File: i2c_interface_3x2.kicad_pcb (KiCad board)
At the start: 2 copper layers, 70.5 x 41.9 mm, 1 part

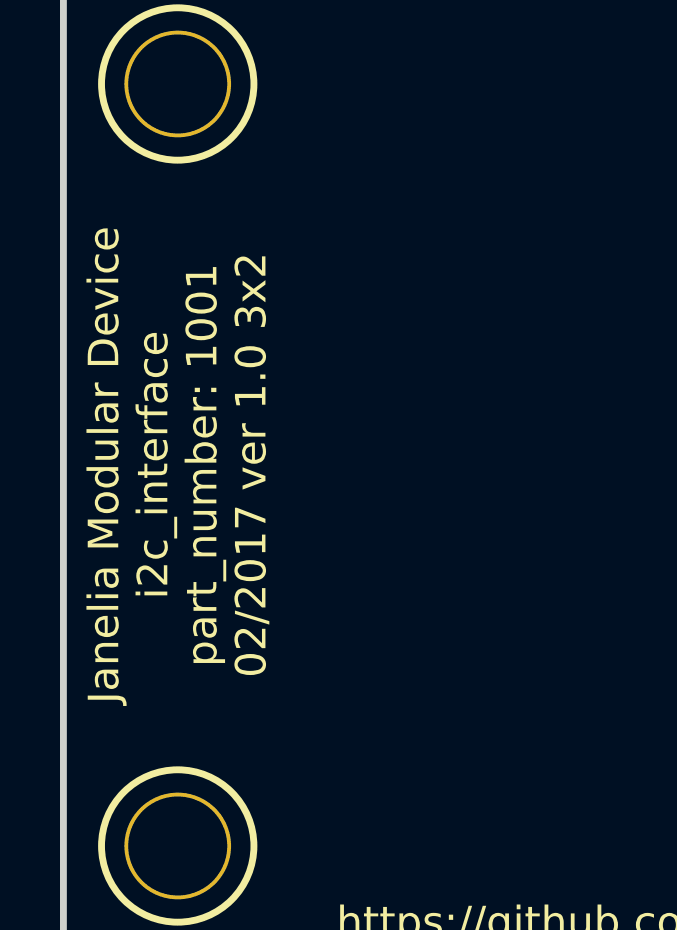
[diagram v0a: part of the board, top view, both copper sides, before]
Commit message: Added footprints.
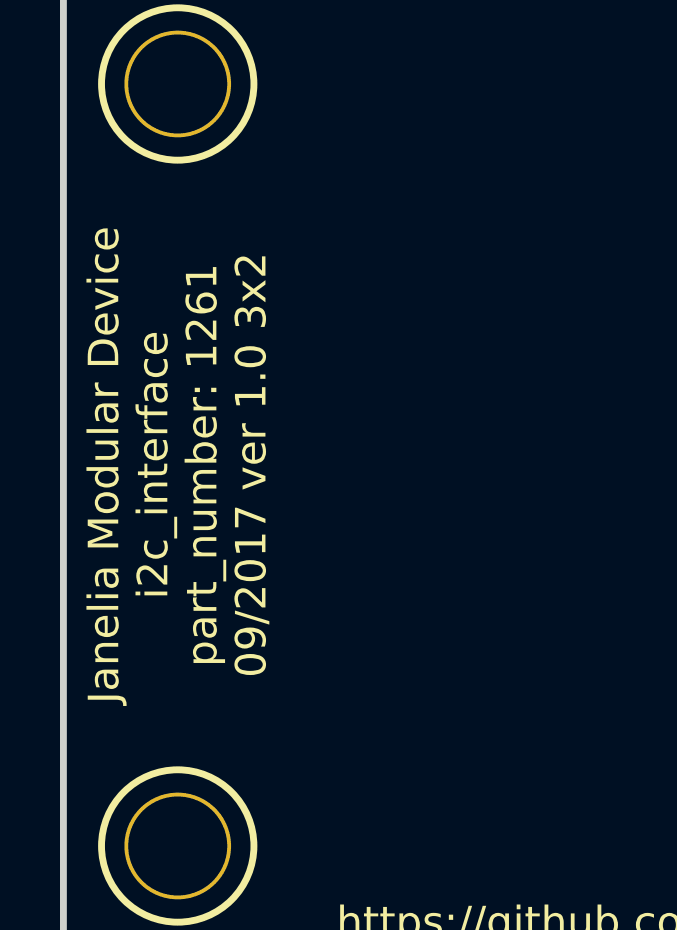
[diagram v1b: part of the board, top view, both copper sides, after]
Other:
- net class Default: trace_width 0.254 -> 0.25
- board text added: "Janelia Modular Device i2c_interface part_number: 1261 09/2017 ver 1.0 3x2"
- board text removed: "Janelia Modular Device i2c_interface part_number: 1001 02/2017 ver 1.0 3x2"
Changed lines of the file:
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@@
-(kicad_pcb (version 20170123) (host pcbnew no-vcs-found-0633d90~59~ubuntu16.04.1)
+(kicad_pcb (version 20170123) (host pcbnew no-vcs-found-e2d3fce~60~ubuntu16.04.1)
   (general
     (thickness 1.6)
@@
   )
   (setup
-    (last_trace_width 0.254)
+    (last_trace_width 0.25)
     (trace_clearance 0.0254)
     (zone_clearance 0.2032)
@@
       (layerselection 0x000f0_ffffffff)
       (usegerberextensions true)
+      (usegerberattributes true)
+      (usegerberadvancedattributes true)
+      (creategerberjobfile true)
       (excludeedgelayer false)
       (linewidth 0.100000)
@@
   (net_class Default "This is the default net class."
     (clearance 0.0254)
-    (trace_width 0.254)
-    (via_dia 0.889)
-    (via_drill 0.635)
-    (uvia_dia 0.508)
-    (uvia_drill 0.127)
-    (diff_pair_gap 0.254)
-    (diff_pair_width 0.254)
+    (trace_width 0.25)
+    (via_dia 0.889)
+    (via_drill 0.635)
+    (uvia_dia 0.508)
+    (uvia_drill 0.127)
   )
   (net_class GND ""
@@
     (effects (font (size 1.016 1.016) (thickness 0.1905)))
   )
-  (gr_text "Janelia Modular Device\ni2c_interface\npart_number: 1001\n02/2017 ver 1.0 3x2" (at 89.535 88.9 90) (layer F.SilkS)
+  (gr_text "Janelia Modular Device\ni2c_interface\npart_number: 1261\n09/2017 ver 1.0 3x2" (at 89.535 88.9 90) (layer F.SilkS)
     (effects (font (size 1.016 1.016) (thickness 0.254)))
   )

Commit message: Progress towards v1.0.
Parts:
- added C1: 0.1uF, i2c_interface_3x2:SM1210, B.Cu at (97.8, 101.0)
- added C2: 0.1uF, i2c_interface_3x2:SM1210, B.Cu at (116.8, 94.6)
- added C3: 10uF, i2c_interface_3x2:SM1210, B.Cu at (109.9, 81.3)
- added P1: HEADER_02X03, i2c_interface_3x2:HEADER_02x03, F.Cu at (101.6, 88.9)
- added P2: HEADER_02X03, i2c_interface_3x2:HEADER_02x03, F.Cu at (118.1, 88.9)
- added R1: 4.7k, i2c_interface_3x2:SM1210, B.Cu at (116.8, 101.0)
- added R2: 4.7k, i2c_interface_3x2:SM1210, B.Cu at (102.9, 101.0)
- added U1: PCA9615, i2c_interface_3x2:TSSOP10, B.Cu at (109.9, 97.8)
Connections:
- MDB1 pad 10: (no net) -> Net-(MDB1-Pad10)
- MDB1 pad 11: (no net) -> Net-(MDB1-Pad11)
- MDB1 pad 12: (no net) -> Net-(MDB1-Pad12)
- MDB1 pad 13: (no net) -> Net-(MDB1-Pad13)
- MDB1 pad 14: (no net) -> Net-(MDB1-Pad14)
- MDB1 pad 15: (no net) -> Net-(MDB1-Pad15)
- MDB1 pad 16: (no net) -> Net-(MDB1-Pad16)
- MDB1 pad 17: (no net) -> Net-(MDB1-Pad17)
- MDB1 pad 18: (no net) -> /SDA
- MDB1 pad 19: (no net) -> /SCL
- MDB1 pad 2: (no net) -> Net-(MDB1-Pad2)
- MDB1 pad 20: (no net) -> Net-(MDB1-Pad20)
- MDB1 pad 21: (no net) -> Net-(MDB1-Pad21)
- MDB1 pad 22: (no net) -> Net-(MDB1-Pad22)
- MDB1 pad 23: (no net) -> Net-(MDB1-Pad23)
- MDB1 pad 24: (no net) -> Net-(MDB1-Pad24)
- MDB1 pad 25: (no net) -> Net-(MDB1-Pad25)
- MDB1 pad 28: (no net) -> Net-(MDB1-Pad28)
- MDB1 pad 29: (no net) -> Net-(MDB1-Pad29)
- MDB1 pad 3: (no net) -> Net-(MDB1-Pad3)
- MDB1 pad 30: (no net) -> Net-(MDB1-Pad30)
- MDB1 pad 3V3: (no net) -> +3V3
- MDB1 pad 4: (no net) -> Net-(MDB1-Pad4)
- MDB1 pad 5: (no net) -> Net-(MDB1-Pad5)
- MDB1 pad 6: (no net) -> Net-(MDB1-Pad6)
- MDB1 pad 9: (no net) -> Net-(MDB1-Pad9)
- MDB1 pad AGND: (no net) -> Net-(MDB1-PadAGND)
- MDB1 pad AREF: (no net) -> Net-(MDB1-PadAREF)
- MDB1 pad DAC: (no net) -> Net-(MDB1-PadDAC)
- MDB1 pad GND: (no net) -> GND
- MDB1 pad VDD: (no net) -> VDD
- MDB1 pad VEE: (no net) -> VEE
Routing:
- net GND: track 0.00 -> 78.6 mm
- net VEE: track 0.00 -> 62.7 mm
- net +3V3: track 0.00 -> 43.2 mm
- net /DSDAM: track 0.00 -> 30.2 mm, vias 0 -> 1
- net /DSCLP: track 0.00 -> 27.4 mm
- net /DSDAP: track 0.00 -> 26.0 mm
- net /DSCLM: track 0.00 -> 25.6 mm
- net /SDA: track 0.00 -> 11.5 mm
- net /SCL: track 0.00 -> 11.5 mm
- added copper zone on B.Cu, net GND
- added copper zone on F.Cu, net VEE
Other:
- net class Default: trace_width 0.25 -> 0.254
- net class GND: trace_width 0.4064 -> 0.3048
- net class POWER: clearance 0.254 -> 0.1016; trace_width 0.8128 -> 0.3048
- net class SIGNAL: trace_width 0.4064 -> 0.3048

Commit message: Modifications.
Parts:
- moved C1 19.9 mm to (115.6, 92.1), turned to 0 degrees
- moved P2 17.7 mm to (101.6, 95.2)
- moved C3 11.2 mm to (101.6, 88.9)
- moved C2 8.98 mm to (115.6, 85.7)
- moved U1 8.89 mm to (109.9, 88.9)
- moved P1 6.35 mm to (101.6, 82.5)
- moved R1 2.54 mm to (114.3, 101.0)
- moved R2 2.54 mm to (105.4, 101.0)
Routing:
- net /DSDAP: track 26.0 -> 44.9 mm
- net GND: track 78.6 -> 59.8 mm
- net VEE: track 62.7 -> 49.2 mm
- net /DSDAM: track 30.2 -> 43.3 mm, vias 1 -> 0
- net /DSCLM: track 25.6 -> 17.7 mm
- net /DSCLP: track 27.4 -> 21.6 mm
- net /SCL: track 11.5 -> 17.1 mm
- net /SDA: track 11.5 -> 17.1 mm
- net +3V3: track 43.2 -> 47.2 mm

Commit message: Finished v1.0.
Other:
- board text added: "T"
- board text added: "TERMINATOR"
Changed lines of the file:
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@@
-(kicad_pcb (version 20170920) (host pcbnew no-vcs-found-b18601d~60~ubuntu16.04.1)
+(kicad_pcb (version 20170920) (host pcbnew no-vcs-found-427e5ec~60~ubuntu16.04.1)
   (general
     (thickness 1.6)
-    (drawings 6)
+    (drawings 81)
     (tracks 140)
     (zones 0)
@@
   (layers
     (0 F.Cu signal)
-    (31 B.Cu signal hide)
+    (31 B.Cu signal)
     (32 B.Adhes user)
     (33 F.Adhes user)
@@
     (pad_to_mask_clearance 0)
     (aux_axis_origin 0 0)
-    (visible_elements FFFFF77F)
+    (visible_elements FFFEF77F)
     (pcbplotparams
       (layerselection 0x000f0_ffffffff)
@@
       (net 3 VEE))
   )
+  (gr_text T (at 144.78 71.12) (layer F.SilkS)
+    (effects (font (size 0.508 0.508) (thickness 0.127)))
+  )
+  (gr_text T (at 141.605 104.14) (layer F.SilkS)
+    (effects (font (size 0.508 0.508) (thickness 0.127)))
+  )
+  (gr_text TERMINATOR (at 141.605 105.41) (layer F.SilkS)
+    (effects (font (size 0.508 0.508) (thickness 0.127)))
+  )
+  (gr_text TERMINATOR (at 147.955 71.12) (layer F.SilkS)
+    (effects (font (size 0.508 0.508) (thickness 0.127)))
+  )
+  (gr_text TERMINATOR (at 110.49 95.25 90) (layer F.SilkS)
+    (effects (font (size 1.016 1.016) (thickness 0.254)))
+  )
+  (gr_line (start 142.24 99.695) (end 150.495 99.695) (angle 90) (layer F.SilkS) (width 0.2286))
+  (gr_line (start 137.795 99.695) (end 140.97 99.695) (angle 90) (layer F.SilkS) (width 0.2286))
+  (gr_line (start 143.51 93.98) (end 143.51 95.25) (angle 90) (layer F.SilkS) (width 0.2286))
+  (gr_line (start 143.51 90.805) (end 143.51 92.71) (angle 90) (layer F.SilkS) (width 0.2286))
+  (gr_line (start 143.51 88.265) (end 143.51 89.535) (angle 90) (layer F.SilkS) (width 0.2286))
+  (gr_line (start 143.51 84.455) (end 143.51 85.725) (angle 90) (layer F.SilkS) (width 0.2286))
+  (gr_line (start 143.51 81.28) (end 143.51 83.185) (angle 90) (layer F.SilkS) (width 0.2286))
+  (gr_line (start 143.51 78.74) (end 143.51 80.01) (angle 90) (layer F.SilkS) (width 0.2286))
+  (gr_line (start 143.51 74.93) (end 143.51 76.2) (angle 90) (layer F.SilkS) (width 0.2286))
+  (gr_line (start 143.51 73.66) (end 143.51 69.215) (angle 90) (layer F.SilkS) (width 0.2286))
+  (gr_line (start 141.605 73.66) (end 144.145 73.66) (angle 90) (layer F.SilkS) (width 0.2286))
+  (gr_line (start 141.605 81.28) (end 141.605 73.66) (angle 90) (layer F.SilkS) (width 0.2286))
+  (gr_line (start 144.145 81.28) (end 141.605 81.28) (angle 90) (layer F.SilkS) (width 0.2286))
+  (gr_line (start 142.875 74.93) (end 144.145 74.93) (angle 90) (layer F.SilkS) (width 0.2286))
+  (gr_line (start 142.875 80.01) (end 142.875 74.93) (angle 90) (layer F.SilkS) (width 0.2286))
+  (gr_line (start 144.145 80.01) (end 142.875 80.01) (angle 90) (layer F.SilkS) (width 0.2286))
+  (gr_line (start 141.605 90.805) (end 144.145 90.805) (angle 90) (layer F.SilkS) (width 0.2286))
+  (gr_line (start 141.605 83.185) (end 141.605 90.805) (angle 90) (layer F.SilkS) (width 0.2286))
+  (gr_line (start 144.145 83.185) (end 141.605 83.185) (angle 90) (layer F.SilkS) (width 0.2286))
+  (gr_line (start 142.875 84.455) (end 144.145 84.455) (angle 90) (layer F.SilkS) (width 0.2286))
+  (gr_line (start 142.875 89.535) (end 142.875 84.455) (angle 90) (layer F.SilkS) (width 0.2286))
+  (gr_line (start 144.145 89.535) (end 142.875 89.535) (angle 90) (layer F.SilkS) (width 0.2286))
+  (gr_line (start 140.97 92.71) (end 140.97 101.6) (angle 90) (layer F.SilkS) (width 0.2286))
+  (gr_line (start 144.145 92.71) (end 140.97 92.71) (angle 90) (layer F.SilkS) (width 0.2286))
+  (gr_line (start 142.24 93.98) (end 144.145 93.98) (angle 90) (layer F.SilkS) (width 0.2286))
+  (gr_line (start 142.24 101.6) (end 142.24 93.98) (angle 90) (layer F.SilkS) (width 0.2286))
+  (gr_line (start 144.145 69.85) (end 144.145 72.39) (angle 90) (layer F.SilkS) (width 0.2286))
+  (gr_line (start 145.415 69.85) (end 145.415 72.39) (angle 90) (layer F.SilkS) (width 0.2286))
+  (gr_line (start 145.415 73.025) (end 145.415 75.565) (angle 90) (layer F.SilkS) (width 0.2286))
+  (gr_line (start 144.145 73.025) (end 144.145 75.565) (angle 90) (layer F.SilkS) (width 0.2286))
+  (gr_line (start 144.145 79.375) (end 144.145 81.915) (angle 90) (layer F.SilkS) (width 0.2286))
+  (gr_line (start 145.415 79.375) (end 145.415 81.915) (angle 90) (layer F.SilkS) (width 0.2286))
+  (gr_line (start 145.415 82.55) (end 145.415 85.09) (angle 90) (layer F.SilkS) (width 0.2286))
+  (gr_line (start 144.145 82.55) (end 144.145 85.09) (angle 90) (layer F.SilkS) (width 0.2286))
+  (gr_line (start 144.145 72.39) (end 145.415 72.39) (angle 90) (layer F.SilkS) (width 0.2286))
+  (gr_line (start 144.145 73.025) (end 145.415 73.025) (angle 90) (layer F.SilkS) (width 0.2286))
+  (gr_line (start 144.145 81.915) (end 145.415 81.915) (angle 90) (layer F.SilkS) (width 0.2286))
+  (gr_line (start 144.145 82.55) (end 145.415 82.55) (angle 90) (layer F.SilkS) (width 0.2286))
+  (gr_line (start 145.415 85.09) (end 144.145 85.09) (angle 90) (layer F.SilkS) (width 0.2286))
+  (gr_line (start 145.415 75.565) (end 144.145 75.565) (angle 90) (layer F.SilkS) (width 0.2286))
+  (gr_line (start 145.415 79.375) (end 144.145 79.375) (angle 90) (layer F.SilkS) (width 0.2286))
+  (gr_line (start 145.415 69.85) (end 144.145 69.85) (angle 90) (layer F.SilkS) (width 0.2286))
+  (gr_line (start 150.495 69.215) (end 150.495 76.2) (angle 90) (layer F.SilkS) (width 0.2286))
+  (gr_line (start 150.495 78.74) (end 150.495 85.725) (angle 90) (layer F.SilkS) (width 0.2286))
+  (gr_line (start 143.51 76.2) (end 150.495 76.2) (angle 90) (layer F.SilkS) (width 0.2286))
+  (gr_line (start 143.51 85.725) (end 150.495 85.725) (angle 90) (layer F.SilkS) (width 0.2286))
+  (gr_line (start 143.51 78.74) (end 150.495 78.74) (angle 90) (layer F.SilkS) (width 0.2286))
+  (gr_line (start 143.51 69.215) (end 150.495 69.215) (angle 90) (layer F.SilkS) (width 0.2286))
+  (gr_line (start 150.495 95.25) (end 143.51 95.25) (angle 90) (layer F.SilkS) (width 0.2286))
+  (gr_line (start 150.495 88.265) (end 150.495 95.25) (angle 90) (layer F.SilkS) (width 0.2286))
+  (gr_line (start 143.51 88.265) (end 150.495 88.265) (angle 90) (layer F.SilkS) (width 0.2286))
+  (gr_line (start 144.145 88.9) (end 144.145 91.44) (angle 90) (layer F.SilkS) (width 0.2286))
+  (gr_line (start 145.415 88.9) (end 144.145 88.9) (angle 90) (layer F.SilkS) (width 0.2286))
+  (gr_line (start 145.415 91.44) (end 145.415 88.9) (angle 90) (layer F.SilkS) (width 0.2286))
+  (gr_line (start 144.145 91.44) (end 145.415 91.44) (angle 90) (layer F.SilkS) (width 0.2286))
+  (gr_line (start 145.415 92.075) (end 144.145 92.075) (angle 90) (layer F.SilkS) (width 0.2286))
+  (gr_line (start 145.415 94.615) (end 145.415 92.075) (angle 90) (layer F.SilkS) (width 0.2286))
+  (gr_line (start 144.145 94.615) (end 145.415 94.615) (angle 90) (layer F.SilkS) (width 0.2286))
+  (gr_line (start 144.145 92.075) (end 144.145 94.615) (angle 90) (layer F.SilkS) (width 0.2286))
+  (gr_line (start 142.875 103.505) (end 140.335 103.505) (angle 90) (layer F.SilkS) (width 0.2286))
+  (gr_line (start 142.875 104.775) (end 142.875 103.505) (angle 90) (layer F.SilkS) (width 0.2286))
+  (gr_line (start 140.335 104.775) (end 142.875 104.775) (angle 90) (layer F.SilkS) (width 0.2286))
+  (gr_line (start 140.335 103.505) (end 140.335 104.775) (angle 90) (layer F.SilkS) (width 0.2286))
+  (gr_line (start 142.875 101.6) (end 140.335 101.6) (angle 90) (layer F.SilkS) (width 0.2286))
+  (gr_line (start 142.875 102.87) (end 142.875 101.6) (angle 90) (layer F.SilkS) (width 0.2286))
+  (gr_line (start 140.335 102.87) (end 142.875 102.87) (angle 90) (layer F.SilkS) (width 0.2286))
+  (gr_line (start 140.335 101.6) (end 140.335 102.87) (angle 90) (layer F.SilkS) (width 0.2286))
+  (gr_line (start 150.495 99.695) (end 150.495 106.68) (angle 90) (layer F.SilkS) (width 0.2286))
+  (gr_line (start 137.795 99.695) (end 137.795 106.68) (angle 90) (layer F.SilkS) (width 0.2286))
+  (gr_line (start 137.795 106.68) (end 150.495 106.68) (angle 90) (layer F.SilkS) (width 0.2286))
   (gr_line (start 156.21 67.945) (end 85.725 67.945) (angle 90) (layer Edge.Cuts) (width 0.2286))
   (gr_line (start 156.21 109.855) (end 156.21 67.945) (angle 90) (layer Edge.Cuts) (width 0.2286))
